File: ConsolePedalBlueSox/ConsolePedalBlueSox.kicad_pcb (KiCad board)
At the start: 2 copper layers, 100 x 60 mm, 52 parts, among them IC1 CD4013BE, J1 Conn_02x25_Counter_Clockwise, Q1 2N3904, Q2 2N3904, Q3 2N3904, U1 RC4558

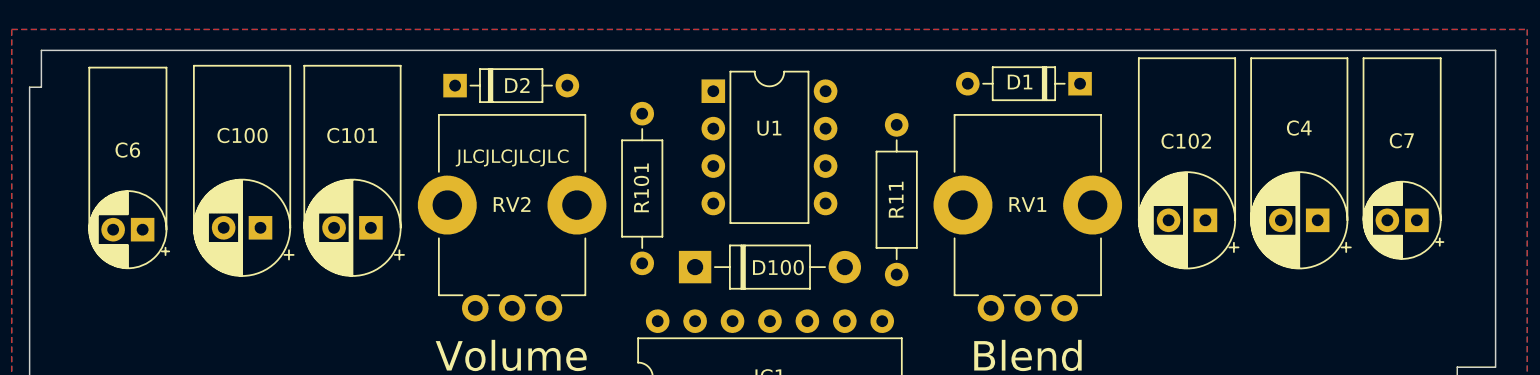
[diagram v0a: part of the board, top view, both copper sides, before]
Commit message: Component placements finalized
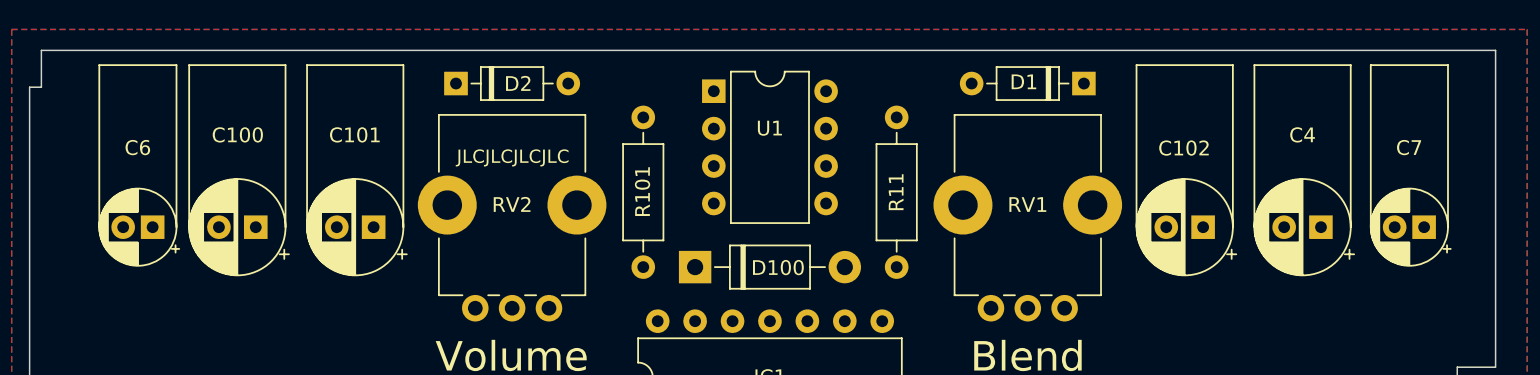
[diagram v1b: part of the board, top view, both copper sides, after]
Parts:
- moved C6 0.70 mm to (90.8, 82.0)
- moved C7 0.68 mm to (177.2, 82.0)
- moved C4 0.52 mm to (170.2, 82.0)
- moved R11 0.51 mm to (141.3, 74.5)
- moved C102 0.49 mm to (162.2, 82.0)
- moved C100 0.32 mm to (97.8, 82.0)
- moved R101 0.26 mm to (124.2, 74.5)
- moved D1 0.26 mm to (154.1, 72.2)
- moved C101 0.19 mm to (105.8, 82.0)
- moved D2 0.15 mm to (111.4, 72.2)
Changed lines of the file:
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@@
   )
   (module libraries:CP_Radial_D6.3mm_P2.50mm (layer F.Cu)
-    (at 169.926 81.534 180)
+    (at 170.15 82 180)
     (descr "CP, Radial series, Radial, pin pitch=2.50mm, , diameter=6.3mm, Electrolytic Capacitor")
     (tags "CP Radial series Radial pin pitch 2.50mm  diameter 6.3mm Electrolytic Capacitor")
@@
   )
   (module libraries:CP_Radial_D5.0mm_P2.00mm_L11.0mm (layer F.Cu)
-    (at 90.17 82.169 180)
+    (at 90.85 82 180)
     (descr "CP, Radial series, Radial, pin pitch=2.00mm, , diameter=5mm, Electrolytic Capacitor")
     (tags "CP Radial series Radial pin pitch 2.00mm  diameter 5mm Electrolytic Capacitor")
@@
   )
   (module libraries:CP_Radial_D5.0mm_P2.00mm_L11.0mm (layer F.Cu)
-    (at 176.657 81.534 180)
+    (at 177.15 82 180)
     (descr "CP, Radial series, Radial, pin pitch=2.00mm, , diameter=5mm, Electrolytic Capacitor")
     (tags "CP Radial series Radial pin pitch 2.00mm  diameter 5mm Electrolytic Capacitor")
@@
   )
   (module libraries:CP_Radial_D6.3mm_P2.50mm_L11.0mm (layer F.Cu)
-    (at 98.171 82.042 180)
+    (at 97.85 82 180)
     (descr "CP, Radial series, Radial, pin pitch=2.50mm, , diameter=6.3mm, Electrolytic Capacitor")
     (tags "CP Radial series Radial pin pitch 2.50mm  diameter 6.3mm Electrolytic Capacitor")
@@
   )
   (module libraries:CP_Radial_D6.3mm_P2.50mm (layer F.Cu)
-    (at 105.664 82.042 180)
+    (at 105.85 82 180)
     (descr "CP, Radial series, Radial, pin pitch=2.50mm, , diameter=6.3mm, Electrolytic Capacitor")
     (tags "CP Radial series Radial pin pitch 2.50mm  diameter 6.3mm Electrolytic Capacitor")
@@
   )
   (module libraries:CP_Radial_D6.3mm_P2.50mm_L11.0mm (layer F.Cu)
-    (at 162.306 81.534 180)
+    (at 162.15 82 180)
     (descr "CP, Radial series, Radial, pin pitch=2.50mm, , diameter=6.3mm, Electrolytic Capacitor")
     (tags "CP Radial series Radial pin pitch 2.50mm  diameter 6.3mm Electrolytic Capacitor")
@@
   )
   (module Diode_THT:D_DO-35_SOD27_P7.62mm_Horizontal (layer F.Cu)
-    (at 153.797 72.263 180)
+    (at 154.06 72.25 180)
     (descr "Diode, DO-35_SOD27 series, Axial, Horizontal, pin pitch=7.62mm, , length*diameter=4*2mm^2, , http://www.diodes.com/_files/packages/DO-35.pdf")
     (tags "Diode DO-35_SOD27 series Axial Horizontal pin pitch 7.62mm  length 4mm diameter 2mm")
@@
   )
   (module Diode_THT:D_DO-35_SOD27_P7.62mm_Horizontal (layer F.Cu)
-    (at 111.379 72.39)
+    (at 111.44 72.25)
     (descr "Diode, DO-35_SOD27 series, Axial, Horizontal, pin pitch=7.62mm, , length*diameter=4*2mm^2, , http://www.diodes.com/_files/packages/DO-35.pdf")
     (tags "Diode DO-35_SOD27 series Axial Horizontal pin pitch 7.62mm  length 4mm diameter 2mm")
@@
   )
   (module Resistor_THT:R_Axial_DIN0207_L6.3mm_D2.5mm_P10.16mm_Horizontal (layer F.Cu)
-    (at 141.351 75.057 270)
+    (at 141.35 74.549 270)
     (descr "Resistor, Axial_DIN0207 series, Axial, Horizontal, pin pitch=10.16mm, 0.25W = 1/4W, length*diameter=6.3*2.5mm^2, http://cdn-reichelt.de/documents/datenblatt/B400/1_4W%23YAG.pdf")
     (tags "Resistor Axial_DIN0207 series Axial Horizontal pin pitch 10.16mm 0.25W = 1/4W length 6.3mm diameter 2.5mm")
@@
   )
   (module Resistor_THT:R_Axial_DIN0207_L6.3mm_D2.5mm_P10.16mm_Horizontal (layer F.Cu)
-    (at 124.079 74.295 270)
+    (at 124.15 74.549 270)
     (descr "Resistor, Axial_DIN0207 series, Axial, Horizontal, pin pitch=10.16mm, 0.25W = 1/4W, length*diameter=6.3*2.5mm^2, http://cdn-reichelt.de/documents/datenblatt/B400/1_4W%23YAG.pdf")
     (tags "Resistor Axial_DIN0207 series Axial Horizontal pin pitch 10.16mm 0.25W = 1/4W length 6.3mm diameter 2.5mm")
@@
   )
   (module Package_DIP:DIP-8_W7.62mm (layer F.Cu)
-    (at 128.905 72.771)
+    (at 128.94 72.771)
     (descr "8-lead though-hole mounted DIP package, row spacing 7.62 mm (300 mils)")
     (tags "THT DIP DIL PDIP 2.54mm 7.62mm 300mil")

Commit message: Finalized and exported board
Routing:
- net /VREF: track 0.00 -> 166.1 mm, vias 0 -> 3
- net Net-(C1-Pad1): track 0.00 -> 152.9 mm, vias 0 -> 2
- net Net-(R7-Pad2): track 0.00 -> 130.7 mm, vias 0 -> 2
- net Net-(C4-Pad1): track 0.00 -> 104.6 mm, vias 0 -> 1
- net Net-(C8-Pad2): track 0.00 -> 100.3 mm, vias 0 -> 1
- net Net-(C3-Pad2): track 0.00 -> 100.2 mm, vias 0 -> 1
- net VDD: track 0.00 -> 78.7 mm
- net Net-(D3-Pad1): track 0.00 -> 67.5 mm
- net Net-(C5-Pad2): track 0.00 -> 66.4 mm, vias 0 -> 1
- net VCC: track 0.00 -> 64.0 mm
- net Net-(C6-Pad2): track 0.00 -> 63.3 mm
- net Net-(C7-Pad1): track 0.00 -> 62.7 mm
- net Net-(C3-Pad1): track 0.00 -> 59.9 mm, vias 0 -> 1
- net Net-(Q2-Pad3): track 0.00 -> 57.3 mm, vias 0 -> 1
- net /CLK2: track 0.00 -> 54.5 mm, vias 0 -> 1
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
